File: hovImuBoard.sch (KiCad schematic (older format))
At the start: 69 parts, among them J1 AVR-ISP-6, J2 Ext. Power, J3 54602-908LF, J4 AVR-JTAG-10, J5 ExtensionPort, U1 LD2981, U2 BMX160, U3 SN65HVD32DR, U4 ATmega1284P-AU, U5 TPS62173DSG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

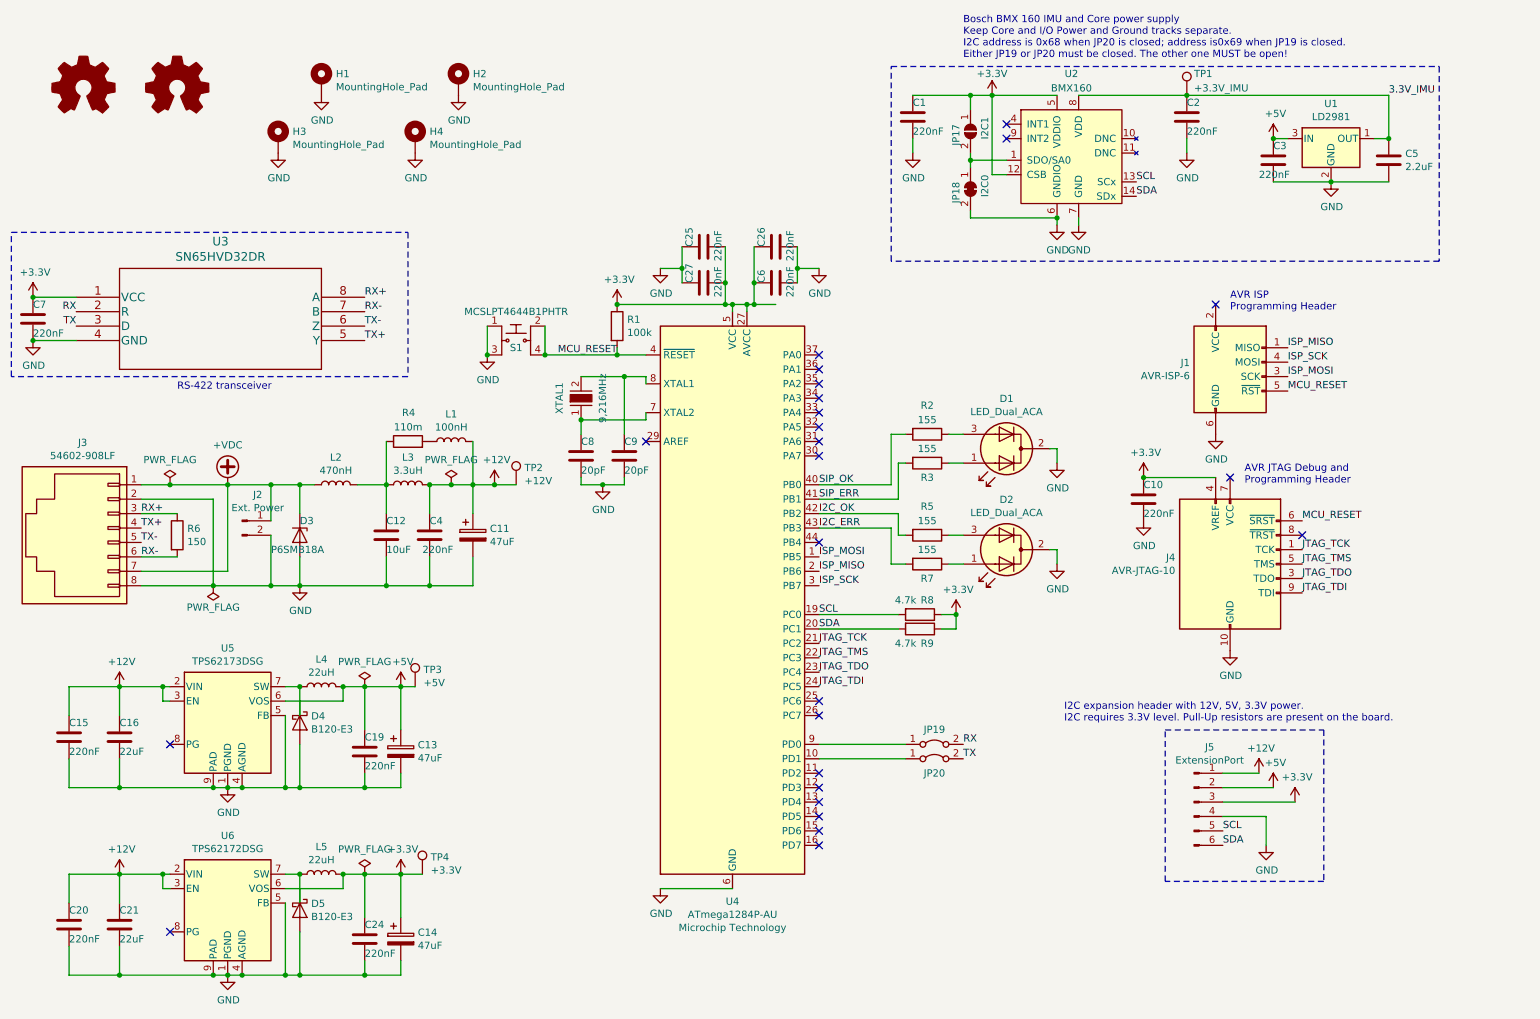
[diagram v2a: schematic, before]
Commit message: Apply corrections from V0.1; Fit board to a plastic box
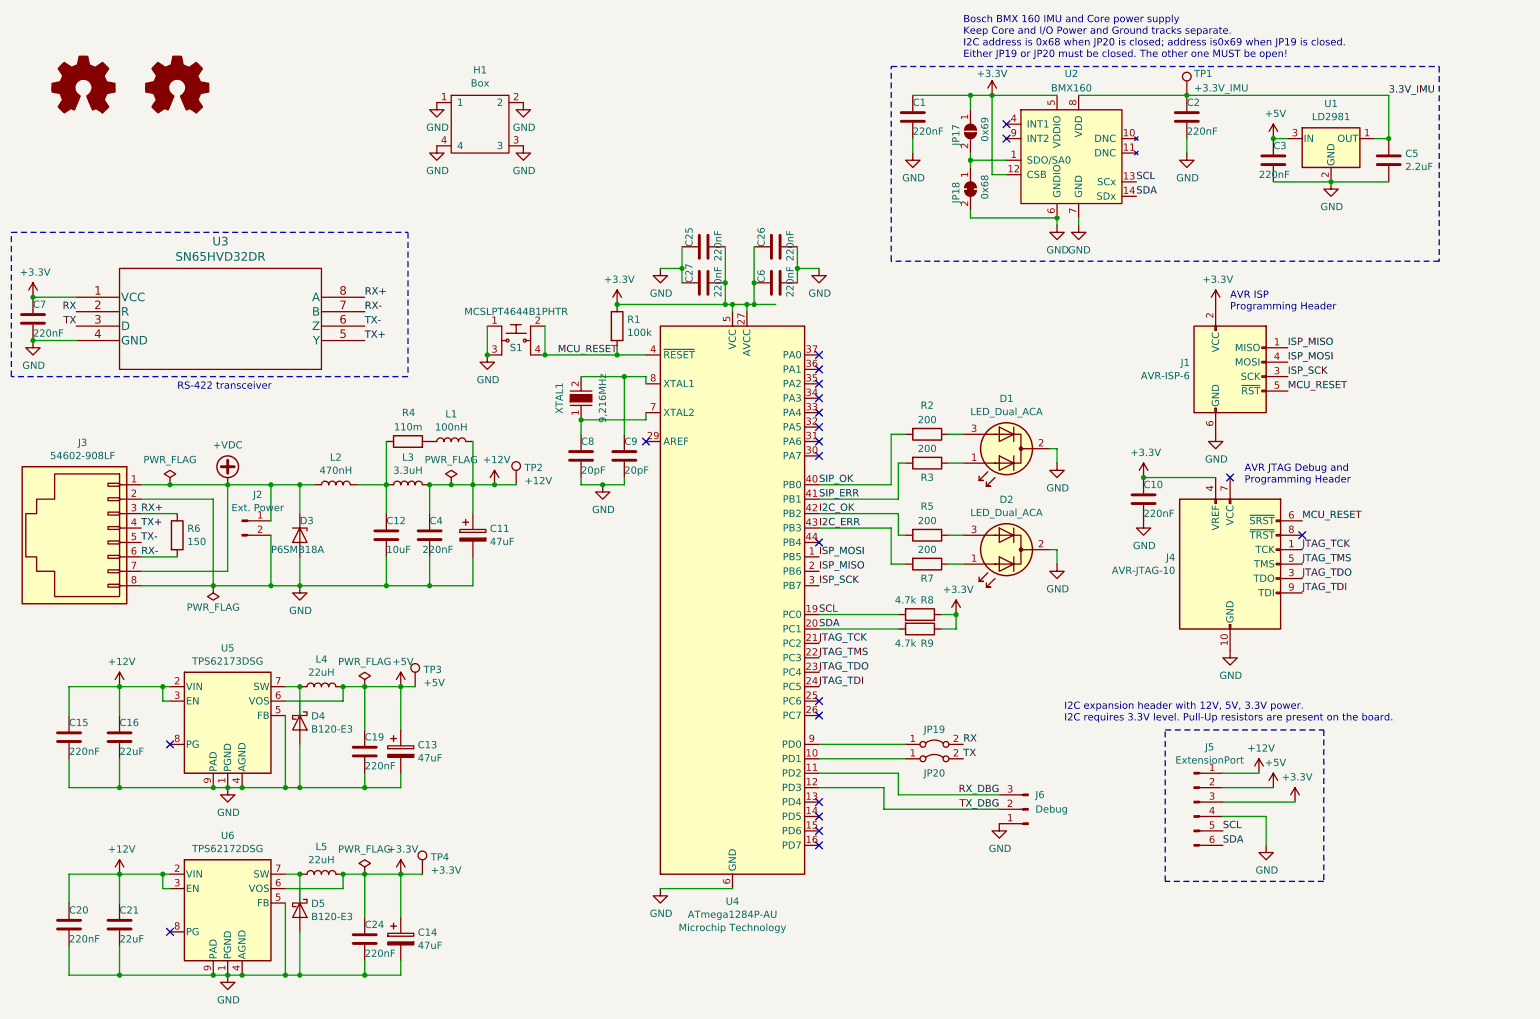
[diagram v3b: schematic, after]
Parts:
- removed H1, H2, H3, H4: MountingHole_Pad, MountingHole:MountingHole_2.7mm_M2.5_Pad_Via, symbol Mechanical:MountingHole_Pad
- added H1: Box, hovImuBoard:Box-CU-1935-MB, symbol hovImuBoard:Box
- added J6: Debug, Connector_PinHeader_2.54mm:PinHeader_1x03_P2.54mm_Vertical, symbol Connector:Conn_01x03_Male
- J4: footprint hovImuBoard:TE_5104338-1 -> digikey-footprints:PinHeader_2x5_P1.27mm_Drill.7mm; Digi-Key_PN A33175-ND -> SAM10711-ND; MPN 5104338-1 -> SHF-105-01-L-D-TH; Manufacturer TE Connectivity AMP Connectors -> Samtec Inc.
- JP17: value I2C1 -> 0x69
- JP18: value I2C0 -> 0x68
- R2, R3, R5, R7: value 155 -> 200; Digi-Key_PN 541-100KCCT-ND -> 541-200CCT-ND; MPN CRCW0805100KFKEA -> CRCW0805200RFKEA
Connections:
- net +3V3: now also J1.2 (VCC)
- net GND: now also H1.1, H1.2, H1.3, H1.4, J6.1 (Pin_1)
- net ISP_MOSI: now also J1.4 (MOSI); no longer J1.3 (SCK)
- net ISP_SCK: now also J1.3 (SCK); no longer J1.4 (MOSI)
- net RX_DBG: now reaches U4.11 (PD2)
- net RX_DBG: now also J6.3 (Pin_3)
- net TX_DBG: now reaches U4.12 (PD3)
- net TX_DBG: now also J6.2 (Pin_2)
- no-connect marks 25 -> 22
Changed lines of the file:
@@
 P 7550 3600
 F 0 "R3" V 7650 3600 50  0000 C CNN
-F 1 "155" V 7450 3600 50  0000 C CNN
+F 1 "200" V 7450 3600 50  0000 C CNN
 F 2 "Resistor_SMD:R_0805_2012Metric" V 7480 3600 50  0001 C CNN
 F 3 "http://www.vishay.com/docs/20035/dcrcwe3.pdf" H 7550 3600 50  0001 C CNN
-F 4 "541-100KCCT-ND" H 7550 3600 50  0001 C CNN "Digi-Key_PN"
-F 5 "CRCW0805100KFKEA" H 7550 3600 50  0001 C CNN "MPN"
+F 4 "541-200CCT-ND" H 7550 3600 50  0001 C CNN "Digi-Key_PN"
+F 5 "CRCW0805200RFKEA" H 7550 3600 50  0001 C CNN "MPN"
 F 6 "Vishay Dale" H 7550 3600 50  0001 C CNN "Manufacturer"
 	1    7550 3600
@@
 F 0 "J4" H 9270 4346 50  0000 R CNN
 F 1 "AVR-JTAG-10" H 9270 4255 50  0000 R CNN
-F 2 "hovImuBoard:TE_5104338-1" V 9500 4450 50  0001 C CNN
-F 3 "~" H 8375 3750 50  0001 C CNN
-F 4 "A33175-ND" H 9650 4300 50  0001 C CNN "Digi-Key_PN"
-F 5 "5104338-1" H 9650 4300 50  0001 C CNN "MPN"
-F 6 "TE Connectivity AMP Connectors" H 9650 4300 50  0001 C CNN "Manufacturer"
+F 2 "digikey-footprints:PinHeader_2x5_P1.27mm_Drill.7mm" V 9500 4450 50  0001 C CNN
+F 3 "http://suddendocs.samtec.com/prints/shf-1xx-01-x-d-xx-xx-mkt.pdf" H 8375 3750 50  0001 C CNN
+F 4 "SAM10711-ND" H 9650 4300 50  0001 C CNN "Digi-Key_PN"
+F 5 "SHF-105-01-L-D-TH" H 9650 4300 50  0001 C CNN "MPN"
+F 6 "Samtec Inc." H 9650 4300 50  0001 C CNN "Manufacturer"
 	1    9650 4300
 	1    0    0    -1
@@
 P 7550 3400
 F 0 "R2" V 7350 3400 50  0000 C CNN
-F 1 "155" V 7450 3400 50  0000 C CNN
+F 1 "200" V 7450 3400 50  0000 C CNN
 F 2 "Resistor_SMD:R_0805_2012Metric" V 7480 3400 50  0001 C CNN
 F 3 "http://www.vishay.com/docs/20035/dcrcwe3.pdf" H 7550 3400 50  0001 C CNN
-F 4 "541-100KCCT-ND" H 7550 3400 50  0001 C CNN "Digi-Key_PN"
-F 5 "CRCW0805100KFKEA" H 7550 3400 50  0001 C CNN "MPN"
+F 4 "541-200CCT-ND" H 7550 3400 50  0001 C CNN "Digi-Key_PN"
+F 5 "CRCW0805200RFKEA" H 7550 3400 50  0001 C CNN "MPN"
 F 6 "Vishay Dale" H 7550 3400 50  0001 C CNN "Manufacturer"
 	1    7550 3400
@@
 P 7550 4100
 F 0 "R5" V 7350 4100 50  0000 C CNN
-F 1 "155" V 7450 4100 50  0000 C CNN
+F 1 "200" V 7450 4100 50  0000 C CNN
 F 2 "Resistor_SMD:R_0805_2012Metric" V 7480 4100 50  0001 C CNN
 F 3 "http://www.vishay.com/docs/20035/dcrcwe3.pdf" H 7550 4100 50  0001 C CNN
-F 4 "541-100KCCT-ND" H 7550 4100 50  0001 C CNN "Digi-Key_PN"
-F 5 "CRCW0805100KFKEA" H 7550 4100 50  0001 C CNN "MPN"
+F 4 "541-200CCT-ND" H 7550 4100 50  0001 C CNN "Digi-Key_PN"
+F 5 "CRCW0805200RFKEA" H 7550 4100 50  0001 C CNN "MPN"
 F 6 "Vishay Dale" H 7550 4100 50  0001 C CNN "Manufacturer"
 	1    7550 4100
@@
 P 7550 4300
 F 0 "R7" V 7650 4300 50  0000 C CNN
-F 1 "155" V 7450 4300 50  0000 C CNN
+F 1 "200" V 7450 4300 50  0000 C CNN
 F 2 "Resistor_SMD:R_0805_2012Metric" V 7480 4300 50  0001 C CNN
 F 3 "http://www.vishay.com/docs/20035/dcrcwe3.pdf" H 7550 4300 50  0001 C CNN
-F 4 "541-100KCCT-ND" H 7550 4300 50  0001 C CNN "Digi-Key_PN"
-F 5 "CRCW0805100KFKEA" H 7550 4300 50  0001 C CNN "MPN"
+F 4 "541-200CCT-ND" H 7550 4300 50  0001 C CNN "Digi-Key_PN"
+F 5 "CRCW0805200RFKEA" H 7550 4300 50  0001 C CNN "MPN"
 F 6 "Vishay Dale" H 7550 4300 50  0001 C CNN "Manufacturer"
 	1    7550 4300
@@
 P 7850 1300
 F 0 "JP17" H 7800 1200 50  0000 L CNN
-F 1 "I2C1" H 7750 1400 50  0000 L CNN
+F 1 "0x69" H 7750 1400 50  0000 L CNN
 F 2 "Jumper:SolderJumper-2_P1.3mm_Open_Pad1.0x1.5mm" H 7850 1300 50  0001 C CNN
 F 3 "~" H 7850 1300 50  0001 C CNN
@@
 P 7850 1700
 F 0 "JP18" H 7800 1600 50  0000 L CNN
-F 1 "I2C0" H 7750 1800 50  0000 L CNN
+F 1 "0x68" H 7750 1800 50  0000 L CNN
 F 2 "Jumper:SolderJumper-2_P1.3mm_Bridged_Pad1.0x1.5mm" H 7850 1700 50  0001 C CNN
 F 3 "~" H 7850 1700 50  0001 C CNN
@@
 ISP_MISO
 Text Label 10050 2900 0    50   ~ 0
+ISP_MOSI
+Text Label 10050 3000 0    50   ~ 0
 ISP_SCK
-Text Label 10050 3000 0    50   ~ 0
-ISP_MOSI
 Text Label 10050 3100 0    50   ~ 0
 MCU_RESET
@@
 	1    0    0    -1
 $EndComp
-NoConn ~ 9550 2500
 Text Notes 9750 3750 0    50   ~ 0
 AVR JTAG Debug and\nProgramming Header
@@
 NoConn ~ 6800 5250
 NoConn ~ 6800 5350
-NoConn ~ 6800 5750
-NoConn ~ 6800 5850
 NoConn ~ 6800 5950
 NoConn ~ 6800 6050
@@
 $EndComp
 $Comp
-L Mechanical:MountingHole_Pad H1
-U 1 1 5D5F84F4
-P 3350 950
-F 0 "H1" H 3450 999 50  0000 L CNN
-F 1 "MountingHole_Pad" H 3450 908 50  0000 L CNN
-F 2 "MountingHole:MountingHole_2.7mm_M2.5_Pad_Via" H 3350 950 50  0001 C CNN
-F 3 "~" H 3350 950 50  0001 C CNN
-	1    3350 950
-	1    0    0    -1
-$EndComp
-$Comp
-L Mechanical:MountingHole_Pad H3
-U 1 1 5D5FB788
-P 3050 1350
-F 0 "H3" H 3150 1399 50  0000 L CNN
-F 1 "MountingHole_Pad" H 3150 1308 50  0000 L CNN
-F 2 "MountingHole:MountingHole_2.7mm_M2.5_Pad_Via" H 3050 1350 50  0001 C CNN
-F 3 "~" H 3050 1350 50  0001 C CNN
-	1    3050 1350
-	1    0    0    -1
-$EndComp
-$Comp
-L Mechanical:MountingHole_Pad H2
-U 1 1 5D5FB92A
-P 4300 950
-F 0 "H2" H 4400 999 50  0000 L CNN
-F 1 "MountingHole_Pad" H 4400 908 50  0000 L CNN
-F 2 "MountingHole:MountingHole_2.7mm_M2.5_Pad_Via" H 4300 950 50  0001 C CNN
-F 3 "~" H 4300 950 50  0001 C CNN
-	1    4300 950
-	1    0    0    -1
-$EndComp
-$Comp
-L Mechanical:MountingHole_Pad H4
-U 1 1 5D5FC33E
-P 4000 1350
-F 0 "H4" H 4100 1399 50  0000 L CNN
-F 1 "MountingHole_Pad" H 4100 1308 50  0000 L CNN
-F 2 "MountingHole:MountingHole_2.7mm_M2.5_Pad_Via" H 4000 1350 50  0001 C CNN
-F 3 "~" H 4000 1350 50  0001 C CNN
-	1    4000 1350
-	1    0    0    -1
-$EndComp
-$Comp
-L power:GND #PWR?
-U 1 1 5D6733FB
-P 3050 1450
-F 0 "#PWR?" H 3050 1200 50  0001 C CNN
-F 1 "GND" H 3055 1277 50  0000 C CNN
-F 2 "" H 3050 1450 50  0001 C CNN
-F 3 "" H 3050 1450 50  0001 C CNN
-	1    3050 1450
-	1    0    0    -1
-$EndComp
-$Comp
-L power:GND #PWR?
-U 1 1 5D673B74
-P 4000 1450
-F 0 "#PWR?" H 4000 1200 50  0001 C CNN
-F 1 "GND" H 4005 1277 50  0000 C CNN
-F 2 "" H 4000 1450 50  0001 C CNN
-F 3 "" H 4000 1450 50  0001 C CNN
-	1    4000 1450
-	1    0    0    -1
-$EndComp
-$Comp
-L power:GND #PWR?
-U 1 1 5D673E04
-P 4300 1050
-F 0 "#PWR?" H 4300 800 50  0001 C CNN
-F 1 "GND" H 4305 877 50  0000 C CNN
-F 2 "" H 4300 1050 50  0001 C CNN
-F 3 "" H 4300 1050 50  0001 C CNN
-	1    4300 1050
-	1    0    0    -1
-$EndComp
-$Comp
-L power:GND #PWR?
-U 1 1 5D673E67
-P 3350 1050
-F 0 "#PWR?" H 3350 800 50  0001 C CNN
-F 1 "GND" H 3355 877 50  0000 C CNN
-F 2 "" H 3350 1050 50  0001 C CNN
-F 3 "" H 3350 1050 50  0001 C CNN
-	1    3350 1050
-	1    0    0    -1
-$EndComp
+L Connector:Conn_01x03_Male J6
+U 1 1 5D725999
+P 8250 6000
+F 0 "J6" H 8200 5900 50  0000 R CNN
+F 1 "Debug" H 8200 6000 50  0000 R CNN
+F 2 "Connector_PinHeader_2.54mm:PinHeader_1x03_P2.54mm_Vertical" H 8250 6000 50  0001 C CNN
+F 3 "~" H 8250 6000 50  0001 C CNN
+	1    8250 6000
+	-1   0    0    1
+$EndComp
+$Comp
+L power:GND #PWR0101
+U 1 1 5D741400
+P 8050 6100
+F 0 "#PWR0101" H 8050 5850 50  0001 C CNN
+F 1 "GND" H 8055 5927 50  0000 C CNN
+F 2 "" H 8050 6100 50  0001 C CNN
+F 3 "" H 8050 6100 50  0001 C CNN
+	1    8050 6100
+	1    0    0    -1
+$EndComp
+Wire Wire Line
+	6800 5750 7350 5750
+Wire Wire Line
+	7350 5750 7350 5900
+Wire Wire Line
+	7350 5900 8050 5900
+Wire Wire Line
+	6800 5850 7250 5850
+Wire Wire Line
+	7250 5850 7250 6000
+Wire Wire Line
+	7250 6000 8050 6000
+Text Label 8050 5900 2    50   ~ 0
+RX_DBG
+Text Label 8050 6000 2    50   ~ 0
+TX_DBG
+$Comp
+L hovImuBoard:Box H1
+U 1 1 5D76E284
+P 4450 1250
+F 0 "H1" H 4450 1625 50  0000 C CNN
+F 1 "Box" H 4450 1534 50  0000 C CNN
+F 2 "hovImuBoard:Box-CU-1935-MB" H 4450 1250 50  0001 C CNN
+F 3 "http://www.budind.com/pdf/hb1935.pdf" H 4450 1250 50  0001 C CNN
+	1    4450 1250
+	1    0    0    -1
+$EndComp
+$Comp
+L power:GND #PWR0102
+U 1 1 5D76E7D6
+P 4150 1100
+F 0 "#PWR0102" H 4150 850 50  0001 C CNN
+F 1 "GND" H 4155 927 50  0000 C CNN
+F 2 "" H 4150 1100 50  0001 C CNN
+F 3 "" H 4150 1100 50  0001 C CNN
+	1    4150 1100
+	1    0    0    -1
+$EndComp
+$Comp
+L power:GND #PWR0103
+U 1 1 5D76EE83
+P 4150 1400
+F 0 "#PWR0103" H 4150 1150 50  0001 C CNN
+F 1 "GND" H 4155 1227 50  0000 C CNN
+F 2 "" H 4150 1400 50  0001 C CNN
+F 3 "" H 4150 1400 50  0001 C CNN
+	1    4150 1400
+	1    0    0    -1
+$EndComp
+$Comp
+L power:GND #PWR0104
+U 1 1 5D76F116
+P 4750 1100
+F 0 "#PWR0104" H 4750 850 50  0001 C CNN
+F 1 "GND" H 4755 927 50  0000 C CNN
+F 2 "" H 4750 1100 50  0001 C CNN
+F 3 "" H 4750 1100 50  0001 C CNN
+	1    4750 1100
+	1    0    0    -1
+$EndComp
+$Comp
+L power:GND #PWR0105
+U 1 1 5D76F534
+P 4750 1400
+F 0 "#PWR0105" H 4750 1150 50  0001 C CNN
+F 1 "GND" H 4755 1227 50  0000 C CNN
+F 2 "" H 4750 1400 50  0001 C CNN
+F 3 "" H 4750 1400 50  0001 C CNN
+	1    4750 1400
+	1    0    0    -1
+$EndComp
+$Comp
+L power:+3.3V #PWR?
+U 1 1 5D75F2E8
+P 9550 2500
+F 0 "#PWR?" H 9550 2350 50  0001 C CNN
+F 1 "+3.3V" H 9565 2673 50  0000 C CNN
+F 2 "" H 9550 2500 50  0001 C CNN
+F 3 "" H 9550 2500 50  0001 C CNN
+	1    9550 2500
+	1    0    0    -1
+$EndComp

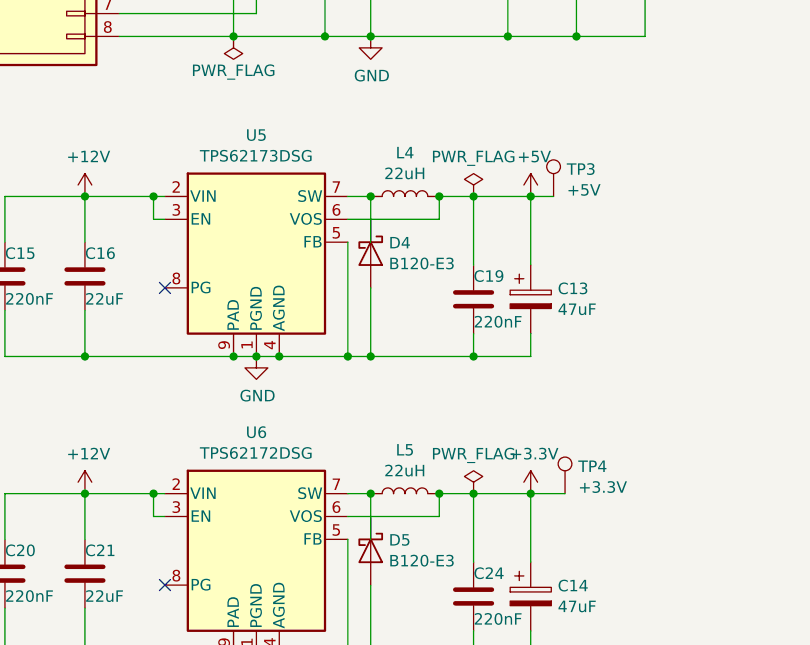
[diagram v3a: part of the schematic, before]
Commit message: Correct L4 and L5 to 2.2uH. Update BOM
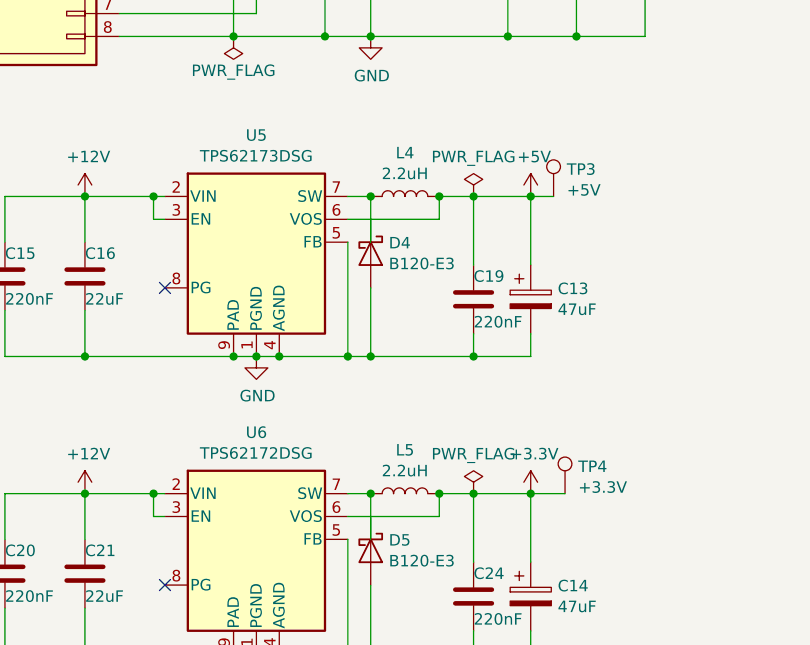
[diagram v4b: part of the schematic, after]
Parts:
- H1: Digi-Key_PN (none) -> 377-1757-ND; MPN (none) -> CU-1935-MB; Manufacturer (none) -> Bud Industries
- L4, L5: value 22uH -> 2.2uH; Category Fixed Inductors -> (none); Description FIXED IND 22UH 1.4A 163.8 MOHM -> (none); Digi-Key_PN 587-3608-1-ND -> 587-2552-1-ND; MPN NRS5040T220MMGKV -> NRS5012T2R2MMGF
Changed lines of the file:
@@
 P 3350 5150
 F 0 "L4" V 3540 5150 50  0000 C CNN
-F 1 "22uH" V 3449 5150 50  0000 C CNN
+F 1 "2.2uH" V 3449 5150 50  0000 C CNN
 F 2 "hovImuBoard:NRS5040T220MMGKV" H 3350 5150 50  0001 C CNN
-F 3 "https://ds.yuden.co.jp/TYCOMPAS/ut/specSheet?pn=NRS5040T220MMGKV++" H 3350 5150 50  0001 C CNN
-F 4 "FIXED IND 22UH 1.4A 163.8 MOHM" H 3350 5150 50  0001 C CNN "Description"
-F 5 "587-3608-1-ND" H 3350 5150 50  0001 C CNN "Digi-Key_PN"
-F 6 "NRS5040T220MMGKV" H 3350 5150 50  0001 C CNN "MPN"
-F 7 "Taiyo Yuden" H 3350 5150 50  0001 C CNN "Manufacturer"
-F 8 "Fixed Inductors" H 3350 5150 50  0001 C CNN "Category"
+F 3 "https://www.yuden.co.jp/productdata/catalog/wound04_e.pdf" H 3350 5150 50  0001 C CNN
+F 4 "587-2552-1-ND" H 3350 5150 50  0001 C CNN "Digi-Key_PN"
+F 5 "NRS5012T2R2MMGF" H 3350 5150 50  0001 C CNN "MPN"
+F 6 "Taiyo Yuden" H 3350 5150 50  0001 C CNN "Manufacturer"
 	1    3350 5150
 	0    -1   -1   0
@@
 P 3350 6450
 F 0 "L5" V 3540 6450 50  0000 C CNN
-F 1 "22uH" V 3449 6450 50  0000 C CNN
+F 1 "2.2uH" V 3449 6450 50  0000 C CNN
 F 2 "hovImuBoard:NRS5040T220MMGKV" H 3350 6450 50  0001 C CNN
-F 3 "https://ds.yuden.co.jp/TYCOMPAS/ut/specSheet?pn=NRS5040T220MMGKV++" H 3350 6450 50  0001 C CNN
-F 4 "FIXED IND 22UH 1.4A 163.8 MOHM" H 3350 6450 50  0001 C CNN "Description"
-F 5 "587-3608-1-ND" H 3350 6450 50  0001 C CNN "Digi-Key_PN"
-F 6 "NRS5040T220MMGKV" H 3350 6450 50  0001 C CNN "MPN"
-F 7 "Taiyo Yuden" H 3350 6450 50  0001 C CNN "Manufacturer"
-F 8 "Fixed Inductors" H 3350 6450 50  0001 C CNN "Category"
+F 3 "https://www.yuden.co.jp/productdata/catalog/wound04_e.pdf" H 3350 6450 50  0001 C CNN
+F 4 "587-2552-1-ND" H 3350 6450 50  0001 C CNN "Digi-Key_PN"
+F 5 "NRS5012T2R2MMGF" H 3350 6450 50  0001 C CNN "MPN"
+F 6 "Taiyo Yuden" H 3350 6450 50  0001 C CNN "Manufacturer"
 	1    3350 6450
 	0    -1   -1   0
@@
 F 2 "hovImuBoard:Box-CU-1935-MB" H 4450 1250 50  0001 C CNN
 F 3 "http://www.budind.com/pdf/hb1935.pdf" H 4450 1250 50  0001 C CNN
+F 4 "377-1757-ND" H 4450 1250 50  0001 C CNN "Digi-Key_PN"
+F 5 "CU-1935-MB" H 4450 1250 50  0001 C CNN "MPN"
+F 6 "Bud Industries" H 4450 1250 50  0001 C CNN "Manufacturer"
 	1    4450 1250
 	1    0    0    -1
@@
 $EndComp
 $Comp
-L power:+3.3V #PWR?
+L power:+3.3V #PWR0106
 U 1 1 5D75F2E8
 P 9550 2500
-F 0 "#PWR?" H 9550 2350 50  0001 C CNN
+F 0 "#PWR0106" H 9550 2350 50  0001 C CNN
 F 1 "+3.3V" H 9565 2673 50  0000 C CNN
 F 2 "" H 9550 2500 50  0001 C CNN
